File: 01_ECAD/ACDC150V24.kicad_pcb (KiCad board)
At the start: 2 copper layers, 85 x 120 mm, 76 parts, among them J1 B2P3-VH(LF)(SN), J2 B4P-VH(LF)(SN), Q1 IXFH20N100P, SW1 NE18 2A EE 6AMP, U1 UCC28600, U2 CNY17-1, U3 TL431DBZ

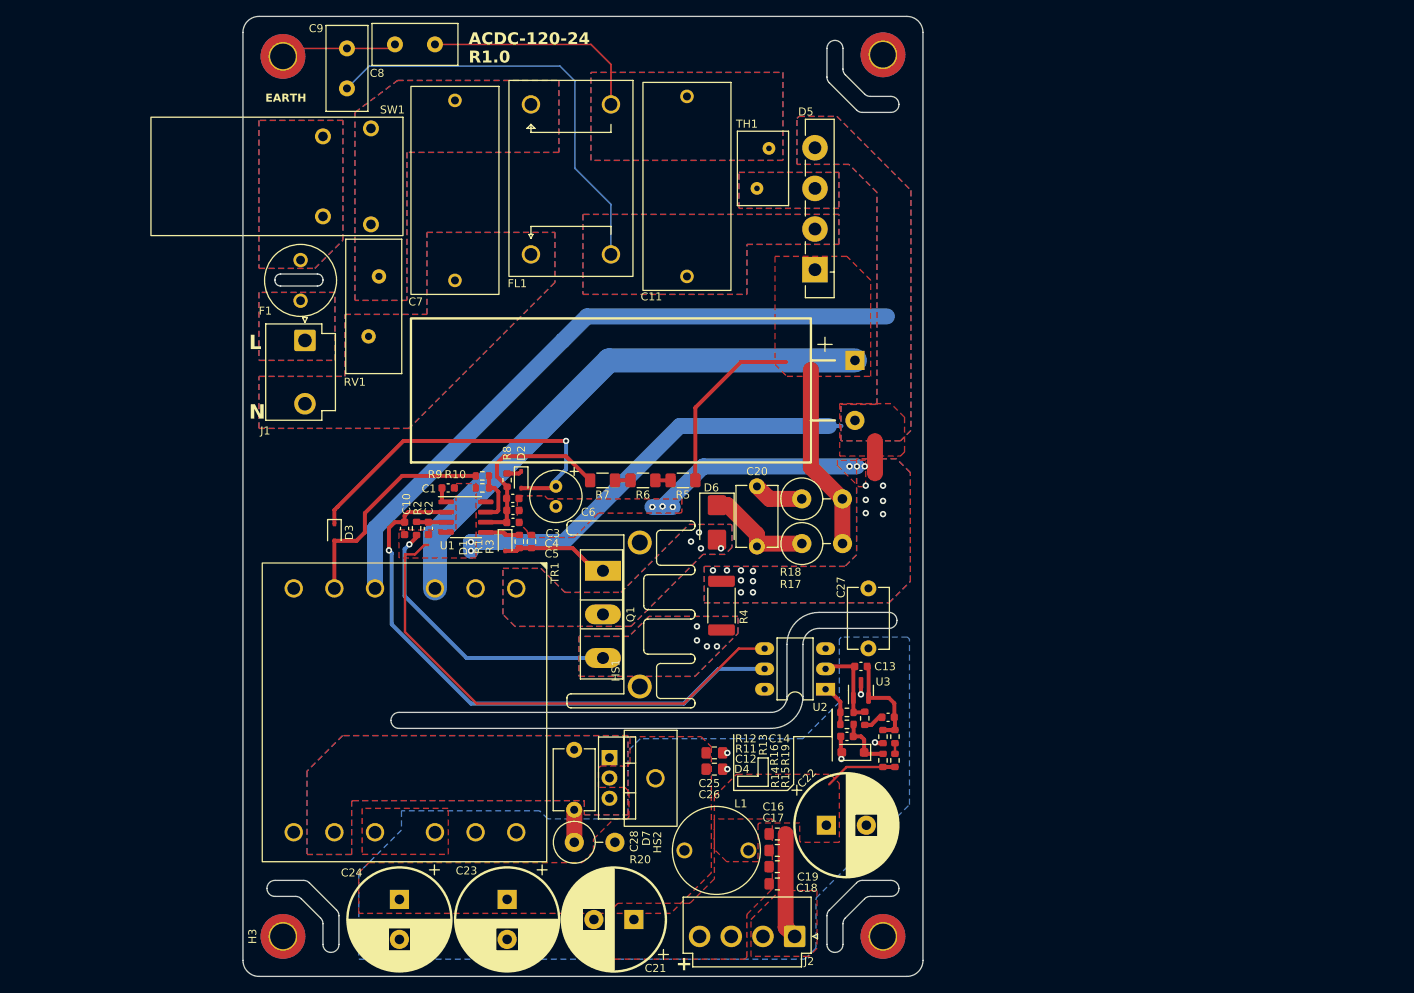
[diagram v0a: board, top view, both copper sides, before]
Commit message: Changing Mosfet.
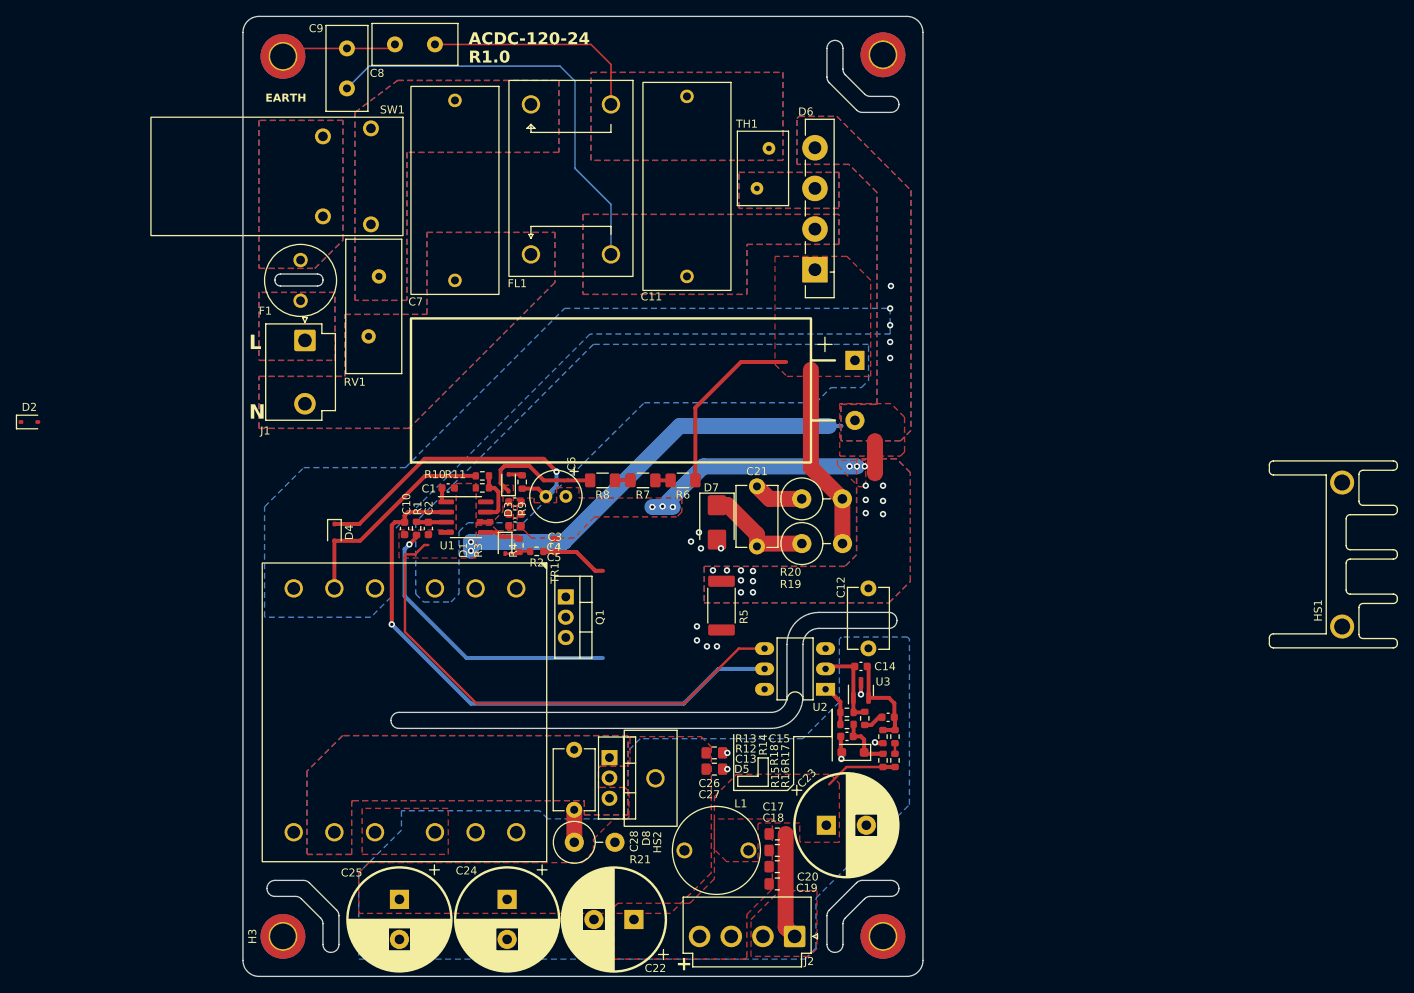
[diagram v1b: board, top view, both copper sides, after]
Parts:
- added D2: PMEG100T10ELXDX, Diode_SMD:D_SOD-323, F.Cu at (6.20, 73.6)
- added R2: 4.7, Resistor_SMD:R_0603_1608Metric, F.Cu at (69.6, 89.8)
- Q1: value IXFH20N100P -> IXFH20N100PSIHA6N80AE-GE3; footprint Package_TO_SOT_THT:TO-247-3_Vertical -> PS:TO-220-3_Vertical
- moved HS1 88.1 mm to (170.3, 99.2)
- moved Q1 5.67 mm to (73.3, 95.5)
- moved R4 2.97 mm to (71.9, 89.0)
- moved R9 1.90 mm to (67.8, 81.1), turned to 90 degrees
- moved C6 1.77 mm to (70.8, 82.9), turned to 0 degrees
- moved D3 1.62 mm to (66.1, 81.2), turned to 90 degrees
- moved C5 0.53 mm to (66.9, 83.6)
- moved C3 0.51 mm to (66.9, 86.6)
- moved C4 0.51 mm to (66.9, 85.1)
- moved R3 0.48 mm to (67.4, 89.0)
- moved D1 0.33 mm to (65.7, 89.0)
- renumbered C27 to C12, C12 to C13, C13 to C14, C14 to C15, C15 to C16, C16 to C17, C17 to C18, C18 to C19, C19 to C20, C20 to C21, C21 to C22, C22 to C23, C23 to C24, C24 to C25, C25 to C26, C26 to C27, D2 to D3, D3 to D4, D4 to D5, D5 to D6, D6 to D7, D7 to D8, R2 to R1, R9 to R10, R10 to R11, R11 to R12, R12 to R13, R13 to R14, R14 to R15, R15 to R16, R19 to R17, R16 to R18, R17 to R19, R18 to R20, R20 to R21, R1 to R3, R3 to R4, R4 to R5, R5 to R6, R6 to R7, R7 to R8, R8 to R9
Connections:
- C3 pad 1: Net-(U1-VDD) -> Net-(D3-K)
- C4 pad 1: Net-(U1-VDD) -> Net-(D3-K)
- C5 pad 1: Net-(U1-VDD) -> Net-(D3-K)
- C6 pad 1: Net-(D2-A) -> Net-(D4-K)
- D3 pad 1: Net-(D2-K) -> Net-(D3-K)
- D3 pad 2: Net-(D2-A) -> Net-(D3-A)
- D4 pad 1: Net-(D2-A) -> Net-(D4-K)
- Q1 pad 1: Net-(D1-A) -> Net-(Q1-G)
- R3 pad 1: Net-(D1-A) -> Net-(Q1-G)
- R3 pad 2: /PS/TR_GAT -> Net-(D2-K)
- R4 pad 1: Net-(D1-A) -> Net-(Q1-G)
- R8 pad 1: Net-(U1-VDD) -> Net-(D3-K)
- R9 pad 1: Net-(D2-K) -> Net-(D4-K)
- R9 pad 2: Net-(U1-VDD) -> Net-(D3-A)
- U1 pad 6: Net-(U1-VDD) -> Net-(D3-K)
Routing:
- net DCR_GND: track 82.5 -> 0.00 mm, vias 0 -> 5
- net /PS/AC_R_O: track 114.4 -> 46.2 mm
- net Net-(D2-A): track 44.7 -> 0.00 mm, vias 1 -> 0
- net Net-(D4-K): track 0.00 -> 38.8 mm, vias 0 -> 1
- net Net-(U1-VDD): track 23.8 -> 0.00 mm
- net Net-(D3-K): track 0.00 -> 15.2 mm
- net Net-(D1-A): track 13.6 -> 3.25 mm
- net Net-(Q1-G): track 0.00 -> 8.46 mm
- net Net-(D2-K): track 1.87 -> 0.00 mm
- net Net-(D3-A): track 0.00 -> 1.75 mm
- net /PS/AUX: track 28.4 -> 27.0 mm
- added copper zone on B.Cu, net /PS/AC_R_O
- added copper zone on F.Cu, net Net-(D2-K)
- removed copper zone on B.Cu, net /PS/TR_SW
- removed copper zone on F.Cu, net /PS/TR_SW
- removed copper zone on B.Cu, net Net-(Q1-S)
- removed copper zone on F.Cu, net Net-(Q1-S)

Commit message: Update.
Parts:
- removed HS1: WV-T247-101E, PS:WV-T247-101E
- added R22: 20k, Resistor_THT:R_Axial_DIN0516_L15.5mm_D5.0mm_P5.08mm_Vertical, F.Cu at (102.4, 86.5)
- Q1: value IXFH20N100PSIHA6N80AE-GE3 -> SIHA6N80AE-GE3; footprint PS:TO-220-3_Vertical -> PS:SIHA6N80AE-GE3
- moved D2 63.1 mm to (67.1, 90.2), turned to 180 degrees
- moved D7 16.5 mm to (82.7, 99.7), turned to 180 degrees
- moved R5 12.7 mm to (83.2, 104.9), turned to 0 degrees
- moved R20 12.3 mm to (90.9, 86.5), turned to 90 degrees
- moved C21 10.5 mm to (87.9, 94.2), turned to 180 degrees
- moved R19 6.52 mm to (96.7, 86.5), turned to 90 degrees
- moved R3 2.97 mm to (70.2, 90.0), turned to 180 degrees
- moved R6 2.12 mm to (86.4, 82.4), turned to 90 degrees
- moved Q1 1.91 mm to (73.5, 97.4)
- moved D1 1.60 mm to (67.1, 88.3), turned to 0 degrees
- moved R7 1.50 mm to (82.9, 82.4), turned to -90 degrees
- moved R2 1.37 mm to (70.2, 88.5)
- moved R4 0.94 mm to (72.6, 88.4)
- moved U2 0.58 mm to (105.7, 106.4)
- moved R8 0.55 mm to (78.4, 80.9)
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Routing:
- net Net-(D7-K): track 13.8 -> 24.4 mm
- net GND_DC_P: track 28.9 -> 39.0 mm, vias 20 -> 18
- net Net-(C21-Pad2): track 6.25 -> 15.4 mm
- net /PS/AC_R_O: track 46.2 -> 53.1 mm
- net Net-(Q1-S): track 36.3 -> 31.5 mm, vias 5 -> 1
- net Net-(Q1-G): track 8.46 -> 11.5 mm
- net Net-(D1-A): track 3.25 -> 1.32 mm
- net GND_DC_S: track 116.5 -> 118.1 mm
- net Net-(R6-Pad1): track 1.90 -> 3.50 mm
- net Net-(D2-K): track 0.00 -> 1.31 mm
- net Net-(R7-Pad1): track 1.95 -> 2.97 mm
- net /PS/TR_GAT: track 4.48 -> 5.07 mm
- added copper zone on B.Cu, net /PS/TR_SW
- added copper zone on F.Cu, net /PS/TR_SW
- added copper zone on F.Cu, net Net-(D3-K)
- added copper zone on F.Cu, net Net-(Q1-S)
- removed copper zone on F.Cu, net Net-(D2-K)
